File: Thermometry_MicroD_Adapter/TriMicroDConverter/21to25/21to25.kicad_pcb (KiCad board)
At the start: 2 copper layers, 71.5 x 8.2 mm, 3 parts, among them J1 Conn_02x02_Odd_Even, J2 DB25_Male, M211 MicroD_21Pin

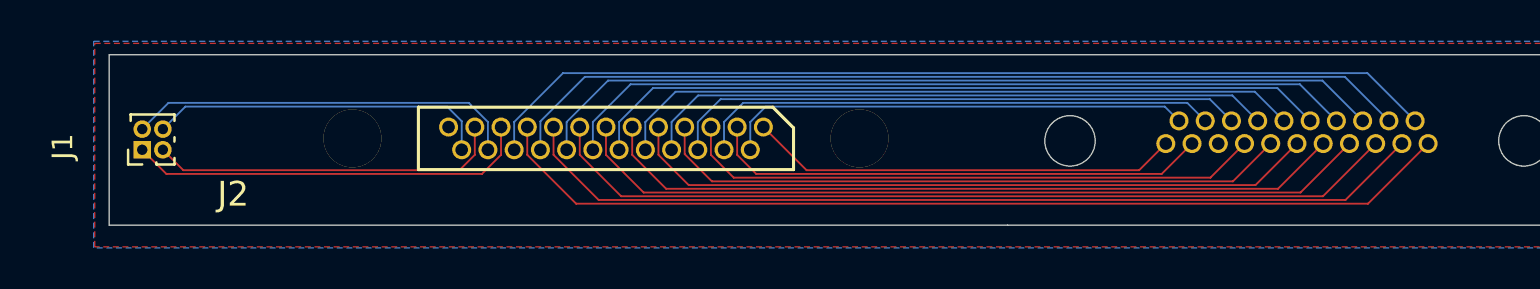
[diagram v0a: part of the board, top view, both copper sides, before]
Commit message: Updated ThermoAdapter
Overlayed +/- traces
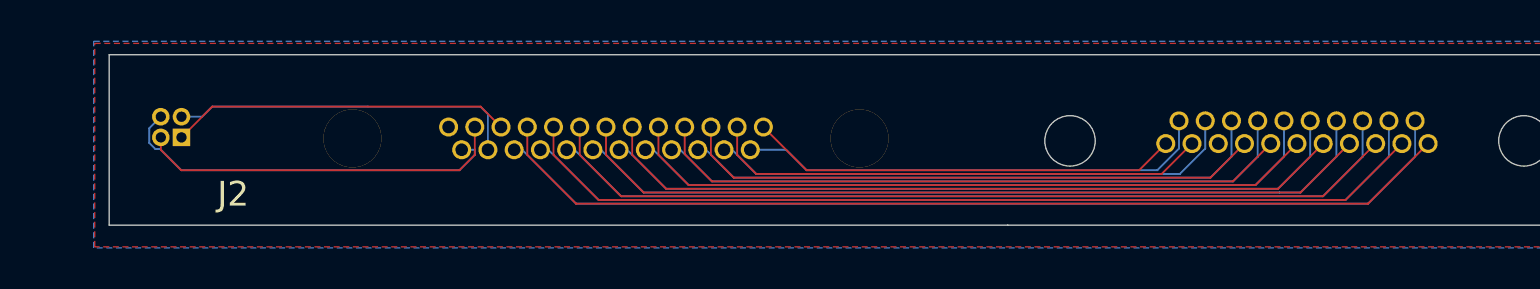
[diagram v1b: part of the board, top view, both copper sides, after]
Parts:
- J1: moved to B.Cu
- moved J1 1.99 mm to (-54.0, 0.00)
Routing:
- net Net-(J1-Pad1): track 19.6 -> 16.5 mm
- net Net-(J1-Pad4): track 16.6 -> 19.0 mm
- net Net-(J1-Pad2): track 19.2 -> 16.9 mm
- net Net-(J1-Pad3): track 17.2 -> 17.9 mm

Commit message: Updated Gerber
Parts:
- J1: moved to F.Cu
- J2 & J3: renamed from J2
- moved J1 1.00 mm to (-55.0, 0.00)
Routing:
- net Net-(J1-Pad4): track 19.0 -> 15.4 mm
- net Net-(J1-Pad1): track 16.5 -> 18.9 mm
- net Net-(J1-Pad3): track 17.9 -> 16.5 mm
- net Net-(J1-Pad2): track 16.9 -> 17.8 mm
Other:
- board text added: "J2 & J3"
- board text added: "TriMicroDConvert_21Pin_V1 August 2021 Ryan Morgenstern"

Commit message: update
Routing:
- net Net-(J1-Pad2): track 17.8 -> 19.4 mm
- net Net-(J1-Pad4): track 15.4 -> 16.7 mm
- net Net-(J1-Pad3): track 16.5 -> 17.5 mm
- net Net-(J1-Pad1): track 18.9 -> 19.9 mm
- net Net-(J2-Pad1): track 20.9 -> 21.7 mm
- net Net-(J2-Pad15): track 25.6 -> 26.1 mm

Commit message: update
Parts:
- removed M211: MicroD_21Pin, Connector:Omnetics_21Pin
- added J10: Conn_01x02, Connector_JST:JST_PH_B2B-PH-K_1x02_P2.00mm_Vertical, F.Cu at (-72.5, 1.11)
- added J11: Conn_01x02, Connector_JST:JST_PH_B2B-PH-K_1x02_P2.00mm_Vertical, F.Cu at (-72.5, -13.9)
- added J3: DB21_Male, 0my_footprints:Omnetics_21Pin, B.Cu at (-6.35, 0.17)
- added J4: Conn_01x02, Connector_JST:JST_PH_B2B-PH-K_1x02_P2.00mm_Vertical, F.Cu at (-66.0, -22.5)
- added J5: Conn_01x02, Connector_JST:JST_PH_B2B-PH-K_1x02_P2.00mm_Vertical, F.Cu at (-66.1, -15.0)
- added J6: Conn_01x02, Connector_JST:JST_PH_B2B-PH-K_1x02_P2.00mm_Vertical, F.Cu at (-66.1, -7.50)
- added J7: Conn_01x02, Connector_JST:JST_PH_B2B-PH-K_1x02_P2.00mm_Vertical, F.Cu at (-66.1, 0.00)
- added J8: Conn_01x02, Connector_JST:JST_PH_B2B-PH-K_1x02_P2.00mm_Vertical, F.Cu at (-72.5, -6.39)
- added J9: Conn_01x02, Connector_JST:JST_PH_B2B-PH-K_1x02_P2.00mm_Vertical, F.Cu at (-72.5, -21.4)
- J2: renamed from J2 & J3
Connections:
- J2 pad 10: Net-(J2-Pad10) -> /10
- J2 pad 22: Net-(J2-Pad22) -> /22
- J2 pad 23: Net-(J2-Pad23) -> /23
- J2 pad 9: Net-(J2-Pad9) -> /9
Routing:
- net /23: track 0.00 -> 155.9 mm
- net /10: track 0.00 -> 150.6 mm
- net /9: track 0.00 -> 141.2 mm
- net /22: track 0.00 -> 98.9 mm
- net Net-(J2-Pad23): track 47.4 -> 0.00 mm
- net Net-(J2-Pad10): track 47.1 -> 0.00 mm
- net Net-(J2-Pad22): track 44.7 -> 0.00 mm
- net Net-(J2-Pad9): track 44.5 -> 0.00 mm
- net Net-(J1-Pad3): track 17.5 -> 19.6 mm
- net Net-(J1-Pad2): track 19.4 -> 21.3 mm
- net Net-(J2-Pad1): track 21.7 -> 23.1 mm
- net Net-(J2-Pad18): track 33.9 -> 35.2 mm
- net Net-(J2-Pad5): track 33.7 -> 34.9 mm
- net Net-(J2-Pad2): track 24.7 -> 25.7 mm
- net Net-(J2-Pad17): track 31.5 -> 32.2 mm
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- added copper zone on B.Cu, net GND
- added copper zone on F.Cu, net GND
- removed copper zone on B.Cu, net (none)
- removed copper zone on F.Cu, net (none)
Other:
- board size 71.5 x 8.2 mm -> 92 x 29.8 mm

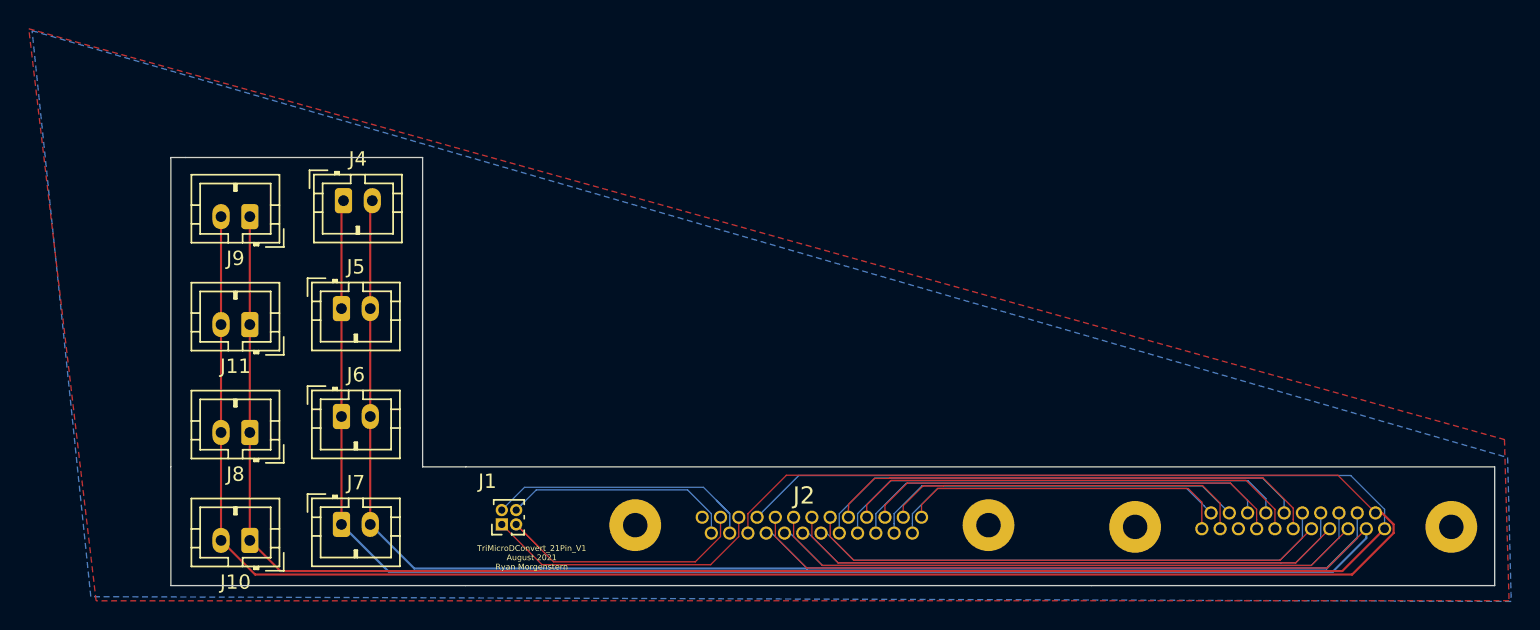
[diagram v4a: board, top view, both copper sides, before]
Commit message: Update
Added current versions of adapter boards.
Added heater line splitter
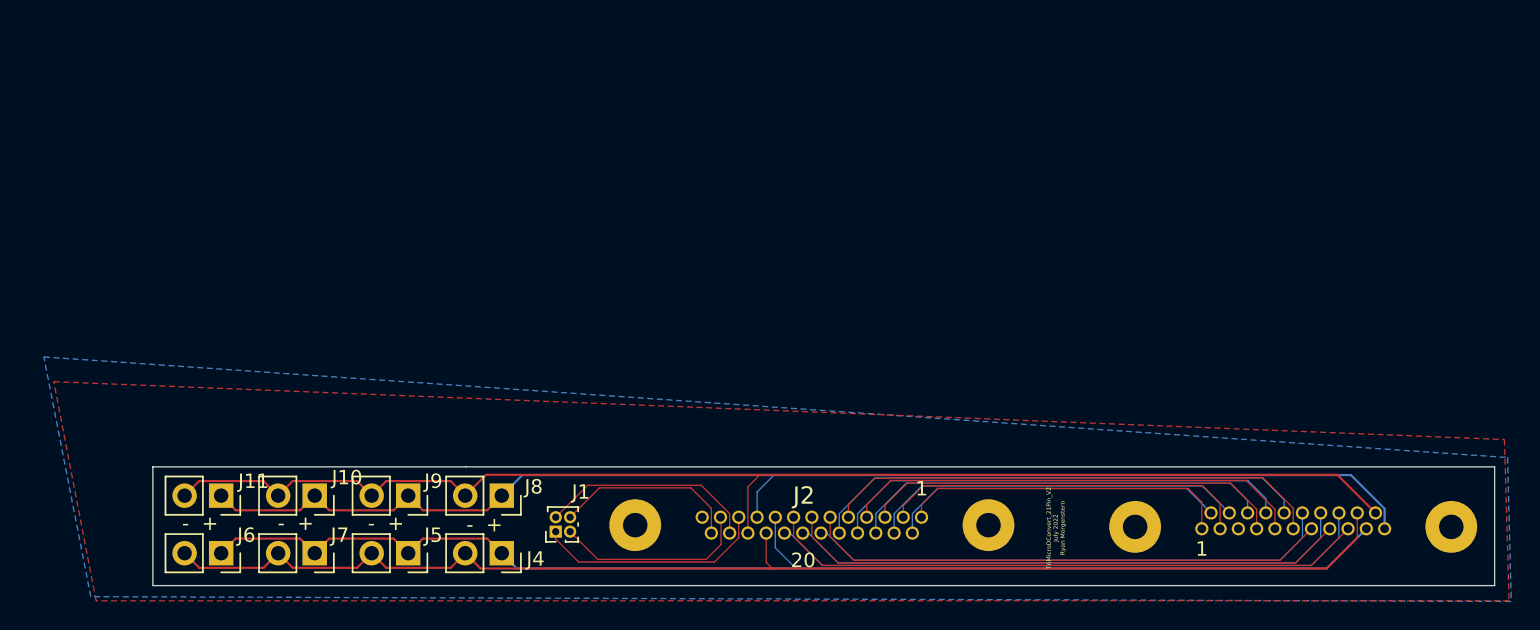
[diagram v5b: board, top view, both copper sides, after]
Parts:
- J10, J11, J4, J5, J6, J7, J8, J9: footprint Connector_JST:JST_PH_B2B-PH-K_1x02_P2.00mm_Vertical -> Connector_PinSocket_2.54mm:PinSocket_1x02_P2.54mm_Vertical
- moved J4 26.9 mm to (-55.0, 2.00), turned to 270 degrees
- moved J9 22.3 mm to (-61.5, -2.00), turned to 270 degrees
- moved J8 18.1 mm to (-55.0, -2.00), turned to 270 degrees
- moved J5 17.6 mm to (-61.5, 2.00), turned to 270 degrees
- moved J6 12.7 mm to (-74.5, 2.00), turned to 270 degrees
- moved J11 12.1 mm to (-74.5, -2.00), turned to 270 degrees
- moved J10 5.48 mm to (-68.0, -2.00), turned to 270 degrees
- moved J1 3.78 mm to (-51.2, 0.50)
- moved J7 2.73 mm to (-68.0, 2.00), turned to 270 degrees
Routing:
- net /23: track 155.9 -> 91.8 mm
- net /10: track 150.6 -> 89.7 mm
- net /9: track 141.2 -> 87.8 mm
- net /22: track 98.9 -> 90.1 mm
- net Net-(J1-Pad2): track 21.3 -> 15.2 mm
- net Net-(J1-Pad3): track 19.6 -> 13.6 mm
- net Net-(J1-Pad4): track 16.9 -> 13.0 mm
- net Net-(J1-Pad1): track 19.8 -> 16.0 mm
- added copper zone on In1.Cu, net GND
- added copper zone on In2.Cu, net GND
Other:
- board size 92 x 29.8 mm -> 93.2 x 8.2 mm
- copper layers 2 -> 4
- board text added: "- +"
- board text added: "1"
- board text added: "20"
- board text added: "TriMicroDConvert_21Pin_V2 July 2022 Ryan Morgenstern"
- board text removed: "TriMicroDConvert_21Pin_V1 August 2021 Ryan Morgenstern"

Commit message: update
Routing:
- net Net-(J2-Pad1): track 23.1 -> 21.1 mm
- net /9: track 87.8 -> 89.5 mm
- net Net-(J1-Pad4): track 13.0 -> 11.6 mm
- net /10: track 89.7 -> 88.5 mm
- net Net-(J2-Pad18): track 35.2 -> 34.1 mm
- net Net-(J2-Pad2): track 25.7 -> 24.6 mm
- net Net-(J2-Pad5): track 34.9 -> 34.0 mm
- net Net-(J2-Pad3): track 29.4 -> 28.6 mm
- net Net-(J2-Pad4): track 32.1 -> 31.3 mm
- net Net-(J2-Pad17): track 32.2 -> 31.4 mm
- net Net-(J2-Pad16): track 29.4 -> 28.7 mm
- net Net-(J1-Pad3): track 13.6 -> 13.1 mm
- removed copper zone on In1.Cu, net GND
- removed copper zone on In2.Cu, net GND
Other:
- copper layers 4 -> 2

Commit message: Update
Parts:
- removed J10, J11, J5, J6, J7, J9: Conn_01x02, Connector_PinSocket_2.54mm:PinSocket_1x02_P2.54mm_Vertical
- moved J4 9.10 mm to (-64.1, 2.00)
- moved J8 9.10 mm to (-64.1, -2.00)
- moved J1 4.20 mm to (-55.5, 0.50)
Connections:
- net /10 renamed Net-(J2-Pad10)
- net /22 renamed Net-(J2-Pad22)
- net /23 renamed Net-(J2-Pad23)
- net /9 renamed Net-(J2-Pad9)
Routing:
- net Net-(J2-Pad9): track 89.5 -> 75.5 mm
- net Net-(J2-Pad23): track 91.9 -> 78.2 mm
- net Net-(J2-Pad10): track 88.5 -> 76.5 mm
- net Net-(J2-Pad22): track 90.3 -> 79.3 mm
- net Net-(J1-Pad4): track 11.6 -> 17.1 mm
- net Net-(J1-Pad3): track 13.1 -> 17.3 mm
- net Net-(J1-Pad2): track 15.1 -> 18.9 mm
- net Net-(J1-Pad1): track 16.1 -> 19.8 mm
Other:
- board size 93.2 x 8.2 mm -> 82.9 x 8.2 mm
